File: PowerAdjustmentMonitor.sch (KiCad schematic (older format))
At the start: 11 parts

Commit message: Power protection and filtering circuit moved to Power.sch, was accidentally on PowerAdjustmentMonitor.sch
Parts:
- removed C? (x2): C, symbol C
- removed F? (x4): FUSE, symbol FUSE
- removed L? (x2): INDUCTOR, symbol INDUCTOR
- removed P?: CONN_12X2, symbol CONN_12X2
- removed R?: R, symbol R
- removed SW?: SWITCH_INV, symbol SWITCH_INV
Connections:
- net labels removed: +12P, +12V, +3.3V, +5V, -12P, -12V, GND
- wire segments 39 -> 0

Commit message: Rough schematic created for power control, conditioning and monitoring circuit
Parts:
- added JP? (x3): JUMPER, symbol JUMPER
- added R? (x8): R, symbol R
- added R? (x2): RVAR, symbol RVAR
- added U? (x2): LM317T, TO-220, symbol LM317T
- added U? (x2): 7805, symbol 7805
- added U? (x2): LM324, symbol LM324
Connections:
- new net: R?.1, R?.2, U?.1 (ADJ)
- new net: R?.2, R?.2, U?.1 (ADJ)
- new net: R?.1, R?.1, U?.3 (IN)
- new net +12V: JP?.1, U?.2 (OUT), U?.4 (V+), U?.4 (V+), U?.VI
- new net -12V: JP?.2, U?.11 (V-), U?.11 (V-), U?.2 (OUT), U?.VO
- new net AGND: JP?.2, R?.1, R?.1, R?.1, R?.1, U?.GND, U?.GND
- new net FE_V+: JP?.2, U?.VO
- new net FE_V-: JP?.1, U?.VI
- new net GND: JP?.1
- new net V+_ADJ: R?.2, R?.2
- new net V+_ADJ_MON: R?.1, R?.2
- new net V+_CURR_MON: U?.1, U?.2 (-)
- new net V+_MON: U?.3 (+)
- new net V-_ADJ: R?.2, R?.2
- new net V-_ADJ_MON: R?.1, R?.2
- new net V-_CURR_MON: U?.1, U?.2 (-)
- new net V-_MON: R?.1, R?.2, U?.3 (+), U?.3 (IN)

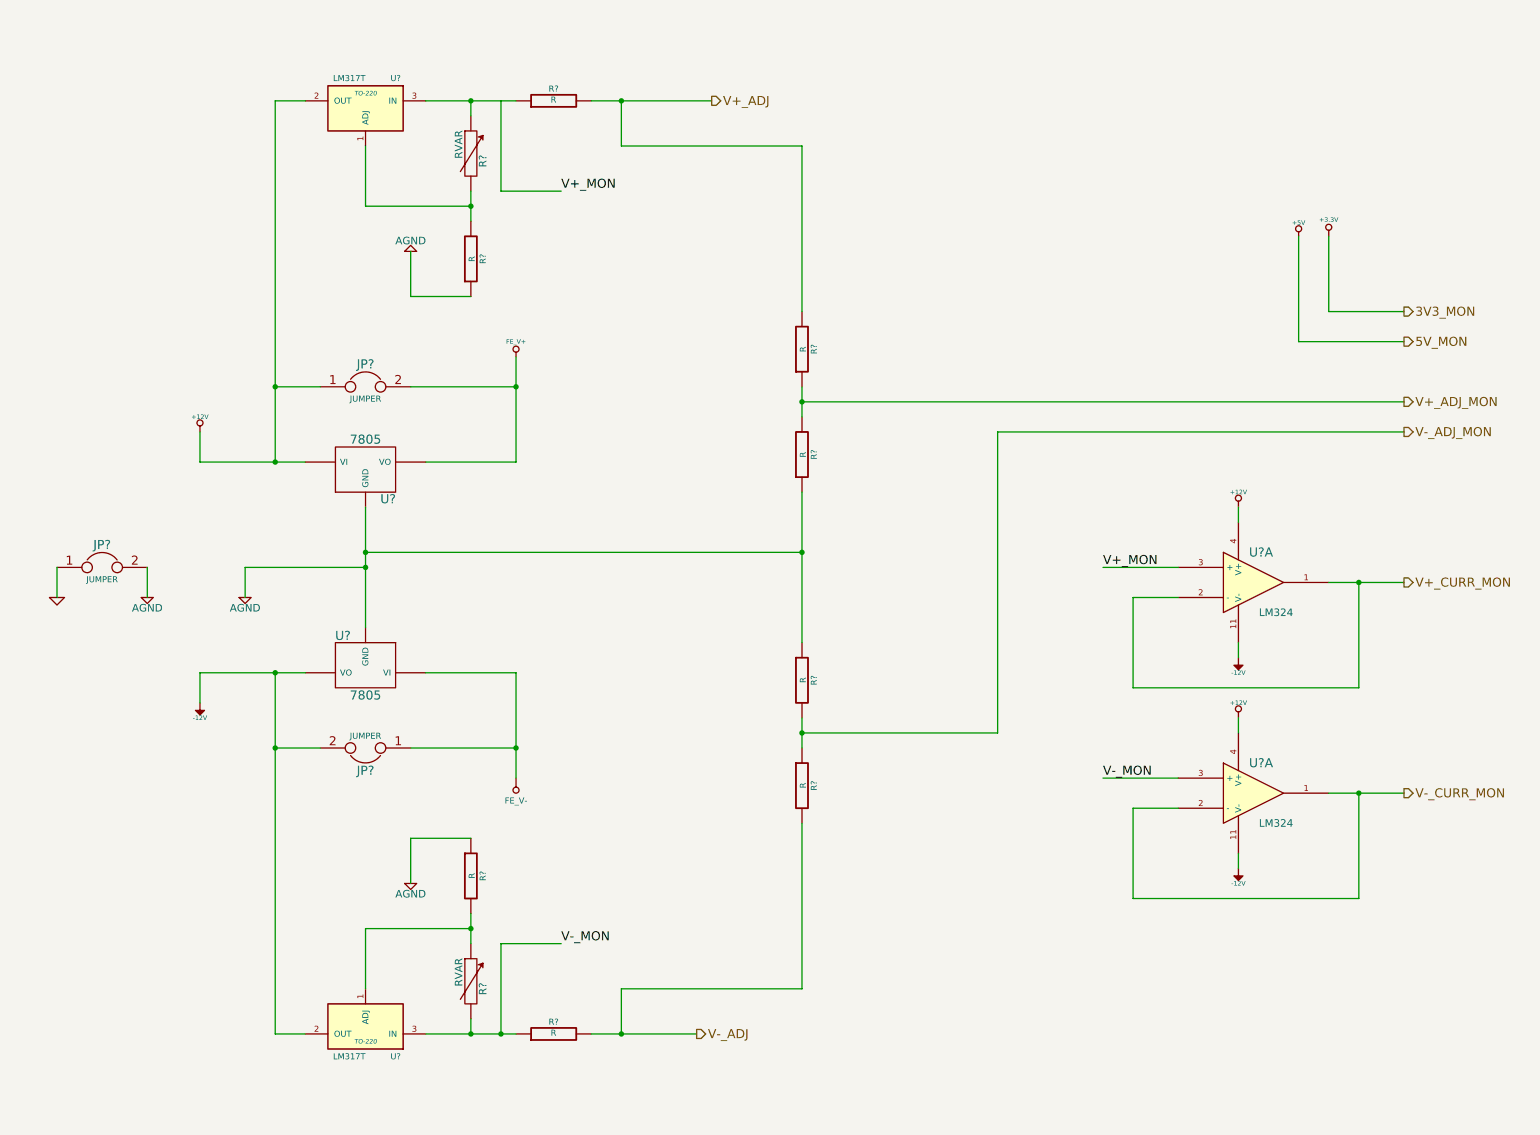
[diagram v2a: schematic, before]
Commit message: Added footprints for the relay module, preliminarily annotated schematic, relay components placed on PCB
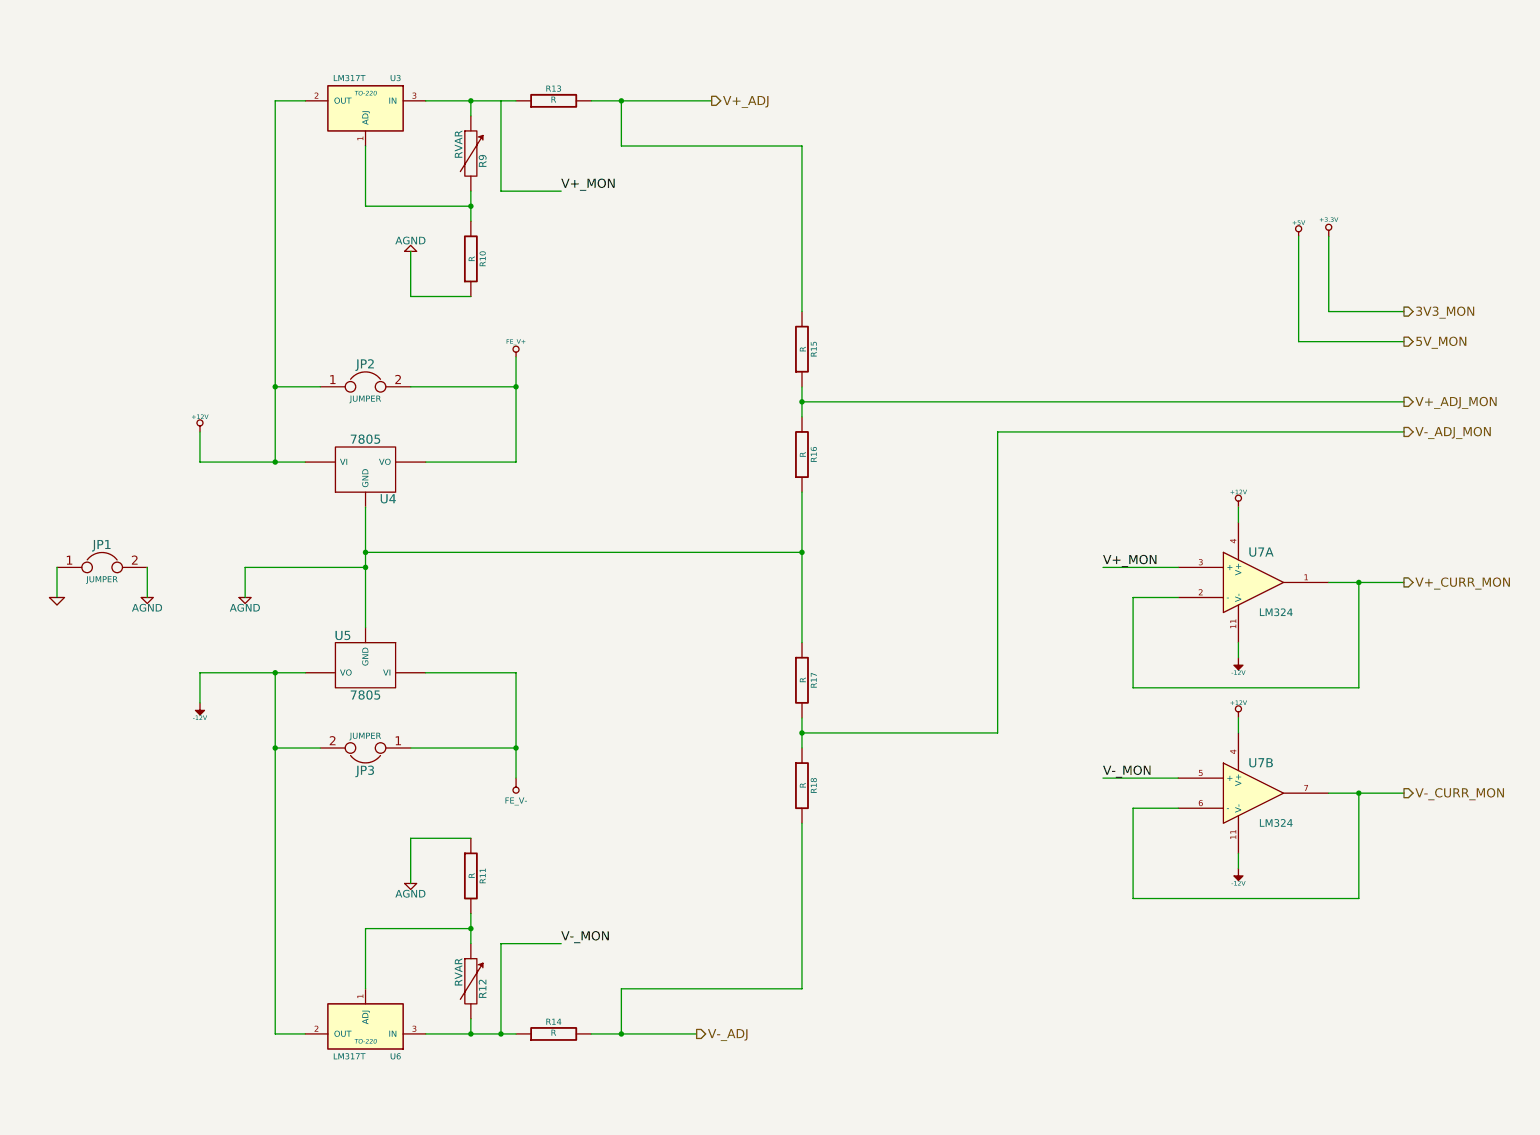
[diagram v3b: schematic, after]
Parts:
- gave numbers to parts that had none: 18
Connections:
- net V-_CURR_MON: now also U7.6 (-), U7.7; no longer U7.1, U7.2 (-)
- net V-_MON: now also U7.5 (+); no longer U7.3 (+)
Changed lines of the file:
@@
 $EndDescr
 $Comp
-L +3.3V #PWR?
+L +3.3V #PWR37
 U 1 1 52F2A379
 P 9700 1900
-F 0 "#PWR?" H 9700 1860 30  0001 C CNN
+F 0 "#PWR37" H 9700 1860 30  0001 C CNN
 F 1 "+3.3V" H 9700 2010 30  0000 C CNN
 F 2 "" H 9700 1900 60  0000 C CNN
@@
 $EndComp
 $Comp
-L +5V #PWR?
+L +5V #PWR36
 U 1 1 52F2A37F
 P 9500 1900
-F 0 "#PWR?" H 9500 1990 20  0001 C CNN
+F 0 "#PWR36" H 9500 1990 20  0001 C CNN
 F 1 "+5V" H 9500 1990 30  0000 C CNN
 F 2 "" H 9500 1900 60  0000 C CNN
@@
 $EndComp
 $Comp
-L +12V #PWR?
+L +12V #PWR25
 U 1 1 52F2A40B
 P 2200 3200
-F 0 "#PWR?" H 2200 3150 20  0001 C CNN
+F 0 "#PWR25" H 2200 3150 20  0001 C CNN
 F 1 "+12V" H 2200 3300 30  0000 C CNN
 F 2 "" H 2200 3200 60  0000 C CNN
@@
 $EndComp
 $Comp
-L -12V #PWR?
+L -12V #PWR26
 U 1 1 52F2A411
 P 2200 5000
-F 0 "#PWR?" H 2200 5130 20  0001 C CNN
+F 0 "#PWR26" H 2200 5130 20  0001 C CNN
 F 1 "-12V" H 2200 5100 30  0000 C CNN
 F 2 "" H 2200 5000 60  0000 C CNN
@@
 $EndComp
 $Comp
-L LM317T U?
+L LM317T U6
 U 1 1 52F2A42B
 P 3300 7150
-F 0 "U?" H 3100 7350 40  0000 C CNN
+F 0 "U6" H 3100 7350 40  0000 C CNN
 F 1 "LM317T" H 3300 7350 40  0000 L CNN
 F 2 "TO-220" H 3300 7250 30  0000 C CIN
@@
 $EndComp
 $Comp
-L JUMPER JP?
+L JUMPER JP2
 U 1 1 52F2A472
 P 3300 2900
-F 0 "JP?" H 3300 3050 60  0000 C CNN
+F 0 "JP2" H 3300 3050 60  0000 C CNN
 F 1 "JUMPER" H 3300 2820 40  0000 C CNN
 F 2 "" H 3300 2900 60  0000 C CNN
@@
 $EndComp
 $Comp
-L JUMPER JP?
+L JUMPER JP3
 U 1 1 52F2A48E
 P 3300 5300
-F 0 "JP?" H 3300 5450 60  0000 C CNN
+F 0 "JP3" H 3300 5450 60  0000 C CNN
 F 1 "JUMPER" H 3300 5220 40  0000 C CNN
 F 2 "" H 3300 5300 60  0000 C CNN
@@
 $EndComp
 $Comp
-L GND #PWR?
+L GND #PWR23
 U 1 1 52F2A4F6
 P 1250 4300
-F 0 "#PWR?" H 1250 4300 30  0001 C CNN
+F 0 "#PWR23" H 1250 4300 30  0001 C CNN
 F 1 "GND" H 1250 4230 30  0001 C CNN
 F 2 "" H 1250 4300 60  0000 C CNN
@@
 $EndComp
 $Comp
-L AGND #PWR?
+L AGND #PWR24
 U 1 1 52F2A718
 P 1850 4300
-F 0 "#PWR?" H 1850 4300 40  0001 C CNN
+F 0 "#PWR24" H 1850 4300 40  0001 C CNN
 F 1 "AGND" H 1850 4230 50  0000 C CNN
 F 2 "" H 1850 4300 60  0000 C CNN
@@
 $EndComp
 $Comp
-L JUMPER JP?
+L JUMPER JP1
 U 1 1 52F2A734
 P 1550 4100
-F 0 "JP?" H 1550 4250 60  0000 C CNN
+F 0 "JP1" H 1550 4250 60  0000 C CNN
 F 1 "JUMPER" H 1550 4020 40  0000 C CNN
 F 2 "" H 1550 4100 60  0000 C CNN
@@
 $EndComp
 $Comp
-L AGND #PWR?
+L AGND #PWR27
 U 1 1 52F2A798
 P 2500 4300
-F 0 "#PWR?" H 2500 4300 40  0001 C CNN
+F 0 "#PWR27" H 2500 4300 40  0001 C CNN
 F 1 "AGND" H 2500 4230 50  0000 C CNN
 F 2 "" H 2500 4300 60  0000 C CNN
@@
 $EndComp
 $Comp
-L FE_V+ #PWR?
+L FE_V+ #PWR30
 U 1 1 52F2A802
 P 4300 2700
-F 0 "#PWR?" H 4300 2800 30  0001 C CNN
+F 0 "#PWR30" H 4300 2800 30  0001 C CNN
 F 1 "FE_V+" H 4300 2800 30  0000 C CNN
 F 2 "" H 4300 2700 60  0000 C CNN
@@
 $EndComp
 $Comp
-L FE_V- #PWR?
+L FE_V- #PWR31
 U 1 1 52F2A839
 P 4300 5500
-F 0 "#PWR?" H 4300 5700 40  0001 C CNN
+F 0 "#PWR31" H 4300 5700 40  0001 C CNN
 F 1 "FE_V-" H 4300 5650 40  0000 C CNN
 F 2 "" H 4300 5500 60  0000 C CNN
@@
 $EndComp
 $Comp
-L 7805 U?
+L 7805 U4
 U 1 1 52F2A885
 P 3300 3450
-F 0 "U?" H 3450 3254 60  0000 C CNN
+F 0 "U4" H 3450 3254 60  0000 C CNN
 F 1 "7805" H 3300 3650 60  0000 C CNN
 F 2 "" H 3300 3450 60  0000 C CNN
@@
 $EndComp
 $Comp
-L 7805 U?
+L 7805 U5
 U 1 1 52F2A8AB
 P 3300 4750
-F 0 "U?" H 3450 4554 60  0000 C CNN
+F 0 "U5" H 3450 4554 60  0000 C CNN
 F 1 "7805" H 3300 4950 60  0000 C CNN
 F 2 "" H 3300 4750 60  0000 C CNN
@@
 $EndComp
 $Comp
-L R R?
+L R R11
 U 1 1 52F2A929
 P 4000 6150
-F 0 "R?" V 4080 6150 40  0000 C CNN
+F 0 "R11" V 4080 6150 40  0000 C CNN
 F 1 "R" V 4007 6151 40  0000 C CNN
 F 2 "" V 3930 6150 30  0000 C CNN
@@
 $EndComp
 $Comp
-L AGND #PWR?
+L AGND #PWR29
 U 1 1 52F2A9E8
 P 3600 6200
-F 0 "#PWR?" H 3600 6200 40  0001 C CNN
+F 0 "#PWR29" H 3600 6200 40  0001 C CNN
 F 1 "AGND" H 3600 6130 50  0000 C CNN
 F 2 "" H 3600 6200 60  0000 C CNN
@@
 $EndComp
 $Comp
-L LM317T U?
+L LM317T U3
 U 1 1 52F2AA95
 P 3300 1050
-F 0 "U?" H 3100 1250 40  0000 C CNN
+F 0 "U3" H 3100 1250 40  0000 C CNN
 F 1 "LM317T" H 3300 1250 40  0000 L CNN
 F 2 "TO-220" H 3300 1150 30  0000 C CIN
@@
 $EndComp
 $Comp
-L R R?
+L R R10
 U 1 1 52F2AAA1
 P 4000 2050
-F 0 "R?" V 4080 2050 40  0000 C CNN
+F 0 "R10" V 4080 2050 40  0000 C CNN
 F 1 "R" V 4007 2051 40  0000 C CNN
 F 2 "" V 3930 2050 30  0000 C CNN
@@
 $EndComp
 $Comp
-L AGND #PWR?
+L AGND #PWR28
 U 1 1 52F2AAAD
 P 3600 2000
-F 0 "#PWR?" H 3600 2000 40  0001 C CNN
+F 0 "#PWR28" H 3600 2000 40  0001 C CNN
 F 1 "AGND" H 3600 1930 50  0000 C CNN
 F 2 "" H 3600 2000 60  0000 C CNN
@@
 V-_CURR_MON
 $Comp
-L R R?
+L R R15
 U 1 1 52F2AC7C
 P 6200 2650
-F 0 "R?" V 6280 2650 40  0000 C CNN
+F 0 "R15" V 6280 2650 40  0000 C CNN
 F 1 "R" V 6207 2651 40  0000 C CNN
 F 2 "" V 6130 2650 30  0000 C CNN
@@
 $EndComp
 $Comp
-L R R?
+L R R16
 U 1 1 52F2AC87
 P 6200 3350
-F 0 "R?" V 6280 3350 40  0000 C CNN
+F 0 "R16" V 6280 3350 40  0000 C CNN
 F 1 "R" V 6207 3351 40  0000 C CNN
 F 2 "" V 6130 3350 30  0000 C CNN
@@
 $EndComp
 $Comp
-L R R?
+L R R18
 U 1 1 52F2AD54
 P 6200 5550
-F 0 "R?" V 6280 5550 40  0000 C CNN
+F 0 "R18" V 6280 5550 40  0000 C CNN
 F 1 "R" V 6207 5551 40  0000 C CNN
 F 2 "" V 6130 5550 30  0000 C CNN
@@
 $EndComp
 $Comp
-L R R?
+L R R17
 U 1 1 52F2AD5A
 P 6200 4850
-F 0 "R?" V 6280 4850 40  0000 C CNN
+F 0 "R17" V 6280 4850 40  0000 C CNN
 F 1 "R" V 6207 4851 40  0000 C CNN
 F 2 "" V 6130 4850 30  0000 C CNN
@@
 	9500 2600 10200 2600
 $Comp
-L R R?
+L R R14
 U 1 1 52F2AED8
 P 4550 7200
-F 0 "R?" V 4630 7200 40  0000 C CNN
+F 0 "R14" V 4630 7200 40  0000 C CNN
 F 1 "R" V 4557 7201 40  0000 C CNN
 F 2 "" V 4480 7200 30  0000 C CNN
@@
 Connection ~ 5000 7200
 $Comp
-L R R?
+L R R13
 U 1 1 52F2B010
 P 4550 1000
-F 0 "R?" V 4630 1000 40  0000 C CNN
+F 0 "R13" V 4630 1000 40  0000 C CNN
 F 1 "R" V 4557 1001 40  0000 C CNN
 F 2 "" V 4480 1000 30  0000 C CNN
@@
 V+_MON
 $Comp
-L LM324 U?
+L LM324 U7
 U 1 1 52F2B56C
 P 9200 4200
-F 0 "U?" H 9250 4400 60  0000 C CNN
+F 0 "U7" H 9250 4400 60  0000 C CNN
 F 1 "LM324" H 9350 4000 50  0000 C CNN
 F 2 "" H 9200 4200 60  0000 C CNN
@@
 $EndComp
 $Comp
-L -12V #PWR?
+L -12V #PWR33
 U 1 1 52F2B572
 P 9100 4700
-F 0 "#PWR?" H 9100 4830 20  0001 C CNN
+F 0 "#PWR33" H 9100 4830 20  0001 C CNN
 F 1 "-12V" H 9100 4800 30  0000 C CNN
 F 2 "" H 9100 4700 60  0000 C CNN
@@
 $EndComp
 $Comp
-L +12V #PWR?
+L +12V #PWR32
 U 1 1 52F2B578
 P 9100 3700
-F 0 "#PWR?" H 9100 3650 20  0001 C CNN
+F 0 "#PWR32" H 9100 3650 20  0001 C CNN
 F 1 "+12V" H 9100 3800 30  0000 C CNN
 F 2 "" H 9100 3700 60  0000 C CNN
@@
 	9100 4600 9100 4700
 $Comp
-L LM324 U?
-U 1 1 52F2B580
+L LM324 U7
+U 2 1 52F2B580
 P 9200 5600
-F 0 "U?" H 9250 5800 60  0000 C CNN
+F 0 "U7" H 9250 5800 60  0000 C CNN
 F 1 "LM324" H 9350 5400 50  0000 C CNN
 F 2 "" H 9200 5600 60  0000 C CNN
 F 3 "" H 9200 5600 60  0000 C CNN
-	1    9200 5600
-	1    0    0    -1
-$EndComp
-$Comp
-L -12V #PWR?
+	2    9200 5600
+	1    0    0    -1
+$EndComp
+$Comp
+L -12V #PWR35
 U 1 1 52F2B586
 P 9100 6100
-F 0 "#PWR?" H 9100 6230 20  0001 C CNN
+F 0 "#PWR35" H 9100 6230 20  0001 C CNN
 F 1 "-12V" H 9100 6200 30  0000 C CNN
 F 2 "" H 9100 6100 60  0000 C CNN
@@
 $EndComp
 $Comp
-L +12V #PWR?
+L +12V #PWR34
 U 1 1 52F2B58C
 P 9100 5100
-F 0 "#PWR?" H 9100 5050 20  0001 C CNN
+F 0 "#PWR34" H 9100 5050 20  0001 C CNN
 F 1 "+12V" H 9100 5200 30  0000 C CNN
 F 2 "" H 9100 5100 60  0000 C CNN
@@
 	10200 3000 6200 3000
 $Comp
-L RVAR R?
+L RVAR R12
 U 1 1 52F2B933
 P 4000 6850
-F 0 "R?" V 4080 6800 50  0000 C CNN
+F 0 "R12" V 4080 6800 50  0000 C CNN
 F 1 "RVAR" V 3920 6910 50  0000 C CNN
 F 2 "" H 4000 6850 60  0000 C CNN
@@
 $EndComp
 $Comp
-L RVAR R?
+L RVAR R9
 U 1 1 52F2B94F
 P 4000 1350
-F 0 "R?" V 4080 1300 50  0000 C CNN
+F 0 "R9" V 4080 1300 50  0000 C CNN
 F 1 "RVAR" V 3920 1410 50  0000 C CNN
 F 2 "" H 4000 1350 60  0000 C CNN
